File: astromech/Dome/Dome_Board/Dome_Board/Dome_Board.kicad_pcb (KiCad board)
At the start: 2 copper layers, 177.8 x 111.8 mm, 12 parts, among them J1 Conn_01x02_Socket, J10 Conn_01x02_Socket, J2 Conn_01x02_Socket, J3 Conn_01x02_Socket, J4 Conn_01x03_Pin, J5 Conn_01x03_Pin, J6 Conn_01x03_Pin, J7 Conn_01x03_Pin, J8 Conn_01x03_Pin, J9 Conn_01x03_Pin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

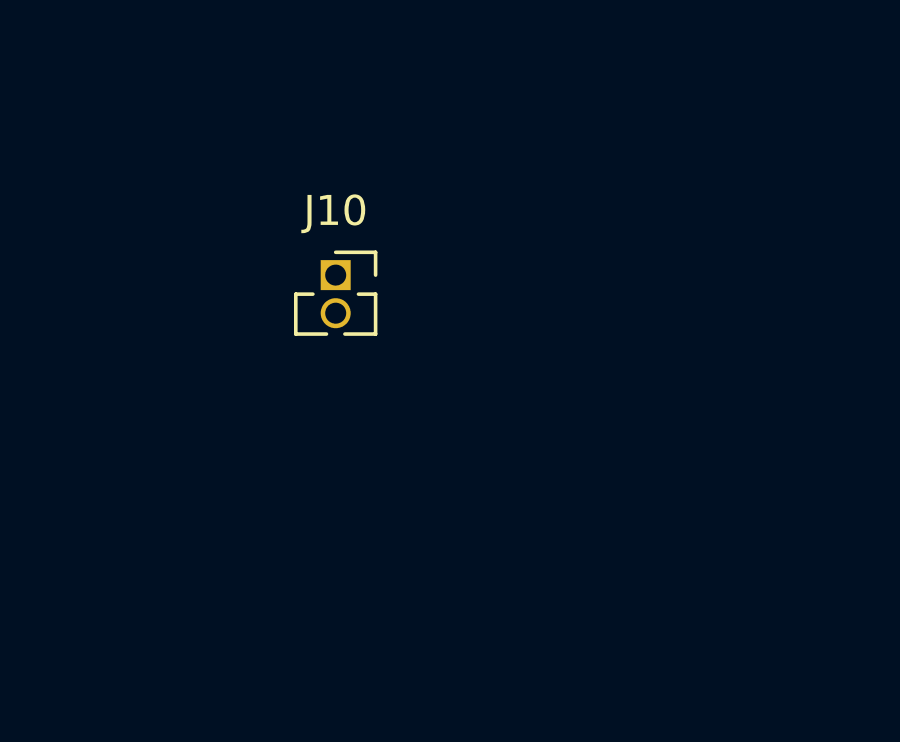
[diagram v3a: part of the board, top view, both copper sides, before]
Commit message: added low power txd, low power rxd, PWM connectors
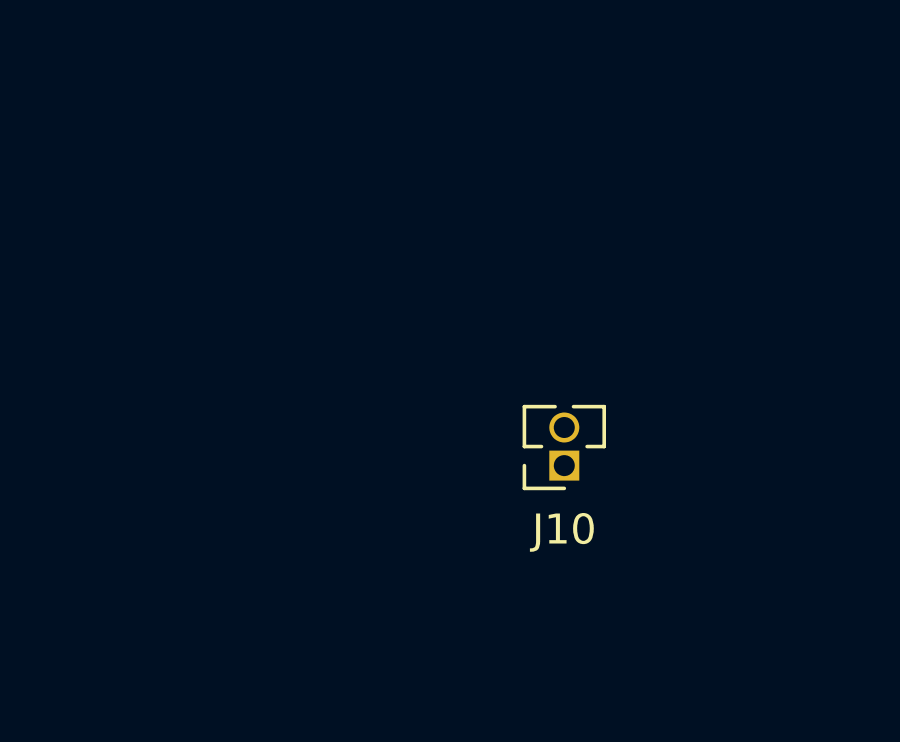
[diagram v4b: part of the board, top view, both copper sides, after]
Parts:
- moved J10 9.92 mm to (147.3, 73.7), turned to 180 degrees
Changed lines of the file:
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@@
 	(footprint "Connector_PinSocket_1.27mm:PinSocket_1x02_P1.27mm_Vertical"
 		(layer "F.Cu")
-		(at 139.7 67.31)
+		(at 147.32 73.66 180)
 		(descr "Through hole straight socket strip, 1x02, 1.27mm pitch, single row (from Kicad 4.0.7), script generated")
 		(tags "Through hole socket strip THT 1x02 1.27mm single row")
 		(property "Reference" "J10"
-			(at 0 -2.135 0)
+			(at 0 -2.135 360)
 			(layer "F.SilkS")
 			(effects
@@
 		)
 		(property "Value" "Conn_01x02_Socket"
-			(at 0 3.405 0)
+			(at 0 3.405 360)
 			(layer "F.Fab")
 			(effects
@@
 		)
 		(property "Footprint" "Connector_PinSocket_1.27mm:PinSocket_1x02_P1.27mm_Vertical"
-			(at 0 0 0)
+			(at 0 0 180)
 			(unlocked yes)
 			(layer "F.Fab")
@@
 		)
 		(property "Datasheet" ""
-			(at 0 0 0)
+			(at 0 0 180)
 			(unlocked yes)
 			(layer "F.Fab")
@@
 		)
 		(property "Description" ""
-			(at 0 0 0)
+			(at 0 0 180)
 			(unlocked yes)
 			(layer "F.Fab")
@@
 		(attr through_hole)
 		(fp_line
+			(start 1.33 0.635)
+			(end 1.33 1.965)
+			(stroke
+				(width 0.12)
+				(type solid)
+			)
+			(layer "F.SilkS")
+		)
+		(fp_line
+			(start 1.33 -0.76)
+			(end 1.33 0)
+			(stroke
+				(width 0.12)
+				(type solid)
+			)
+			(layer "F.SilkS")
+		)
+		(fp_line
+			(start 0.76 0.635)
+			(end 1.33 0.635)
+			(stroke
+				(width 0.12)
+				(type solid)
+			)
+			(layer "F.SilkS")
+		)
+		(fp_line
+			(start 0.30753 1.965)
+			(end 1.33 1.965)
+			(stroke
+				(width 0.12)
+				(type solid)
+			)
+			(layer "F.SilkS")
+		)
+		(fp_line
+			(start 0 -0.76)
+			(end 1.33 -0.76)
+			(stroke
+				(width 0.12)
+				(type solid)
+			)
+			(layer "F.SilkS")
+		)
+		(fp_line
+			(start -1.33 1.965)
+			(end -0.30753 1.965)
+			(stroke
+				(width 0.12)
+				(type solid)
+			)
+			(layer "F.SilkS")
+		)
+		(fp_line
+			(start -1.33 0.635)
+			(end -0.76 0.635)
+			(stroke
+				(width 0.12)
+				(type solid)
+			)
+			(layer "F.SilkS")
+		)
+		(fp_line
 			(start -1.33 0.635)
 			(end -1.33 1.965)
@@
 		)
 		(fp_line
-			(start -1.33 0.635)
-			(end -0.76 0.635)
-			(stroke
-				(width 0.12)
-				(type solid)
-			)
-			(layer "F.SilkS")
-		)
-		(fp_line
-			(start -1.33 1.965)
-			(end -0.30753 1.965)
-			(stroke
-				(width 0.12)
-				(type solid)
-			)
-			(layer "F.SilkS")
-		)
-		(fp_line
-			(start 0 -0.76)
-			(end 1.33 -0.76)
-			(stroke
-				(width 0.12)
-				(type solid)
-			)
-			(layer "F.SilkS")
-		)
-		(fp_line
-			(start 0.30753 1.965)
-			(end 1.33 1.965)
-			(stroke
-				(width 0.12)
-				(type solid)
-			)
-			(layer "F.SilkS")
-		)
-		(fp_line
-			(start 0.76 0.635)
-			(end 1.33 0.635)
-			(stroke
-				(width 0.12)
-				(type solid)
-			)
-			(layer "F.SilkS")
-		)
-		(fp_line
-			(start 1.33 -0.76)
-			(end 1.33 0)
-			(stroke
-				(width 0.12)
-				(type solid)
-			)
-			(layer "F.SilkS")
-		)
-		(fp_line
-			(start 1.33 0.635)
-			(end 1.33 1.965)
-			(stroke
-				(width 0.12)
-				(type solid)
-			)
-			(layer "F.SilkS")
+			(start 1.75 2.4)
+			(end -1.8 2.4)
+			(stroke
+				(width 0.05)
+				(type solid)
+			)
+			(layer "F.CrtYd")
+		)
+		(fp_line
+			(start 1.75 -1.15)
+			(end 1.75 2.4)
+			(stroke
+				(width 0.05)
+				(type solid)
+			)
+			(layer "F.CrtYd")
+		)
+		(fp_line
+			(start -1.8 2.4)
+			(end -1.8 -1.15)
+			(stroke
+				(width 0.05)
+				(type solid)
+			)
+			(layer "F.CrtYd")
 		)
 		(fp_line
@@
 		)
 		(fp_line
-			(start -1.8 2.4)
-			(end -1.8 -1.15)
-			(stroke
-				(width 0.05)
-				(type solid)
-			)
-			(layer "F.CrtYd")
-		)
-		(fp_line
-			(start 1.75 -1.15)
-			(end 1.75 2.4)
-			(stroke
-				(width 0.05)
-				(type solid)
-			)
-			(layer "F.CrtYd")
-		)
-		(fp_line
-			(start 1.75 2.4)
-			(end -1.8 2.4)
-			(stroke
-				(width 0.05)
-				(type solid)
-			)
-			(layer "F.CrtYd")
+			(start 1.27 1.905)
+			(end -1.27 1.905)
+			(stroke
+				(width 0.1)
+				(type solid)
+			)
+			(layer "F.Fab")
+		)
+		(fp_line
+			(start 1.27 0)
+			(end 1.27 1.905)
+			(stroke
+				(width 0.1)
+				(type solid)
+			)
+			(layer "F.Fab")
+		)
+		(fp_line
+			(start 0.635 -0.635)
+			(end 1.27 0)
+			(stroke
+				(width 0.1)
+				(type solid)
+			)
+			(layer "F.Fab")
+		)
+		(fp_line
+			(start -1.27 1.905)
+			(end -1.27 -0.635)
+			(stroke
+				(width 0.1)
+				(type solid)
+			)
+			(layer "F.Fab")
 		)
 		(fp_line
@@
 			(layer "F.Fab")
 		)
-		(fp_line
-			(start -1.27 1.905)
-			(end -1.27 -0.635)
-			(stroke
-				(width 0.1)
-				(type solid)
-			)
-			(layer "F.Fab")
-		)
-		(fp_line
-			(start 0.635 -0.635)
-			(end 1.27 0)
-			(stroke
-				(width 0.1)
-				(type solid)
-			)
-			(layer "F.Fab")
-		)
-		(fp_line
-			(start 1.27 0)
-			(end 1.27 1.905)
-			(stroke
-				(width 0.1)
-				(type solid)
-			)
-			(layer "F.Fab")
-		)
-		(fp_line
-			(start 1.27 1.905)
-			(end -1.27 1.905)
-			(stroke
-				(width 0.1)
-				(type solid)
-			)
-			(layer "F.Fab")
-		)
 		(fp_text user "${REFERENCE}"
 			(at 0 0.635 90)
@@
 		)
 		(pad "1" thru_hole rect
-			(at 0 0)
+			(at 0 0 180)
 			(size 1 1)
 			(drill 0.7)
@@
 		)
 		(pad "2" thru_hole oval
-			(at 0 1.27)
+			(at 0 1.27 180)
 			(size 1 1)
 			(drill 0.7)

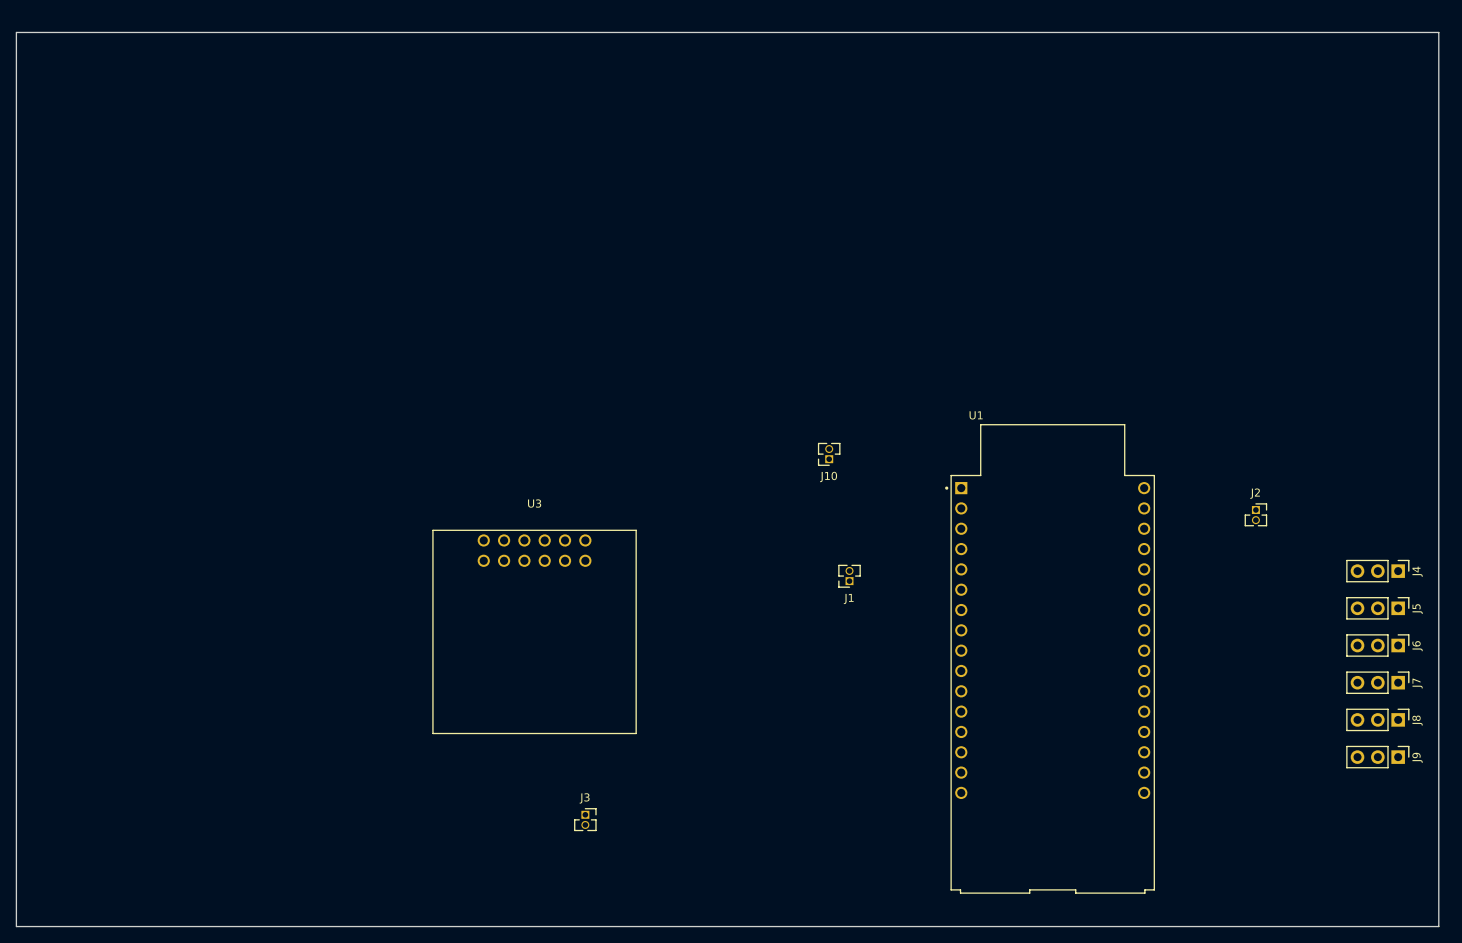
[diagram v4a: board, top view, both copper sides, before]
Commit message: added more PWM and Servo driver
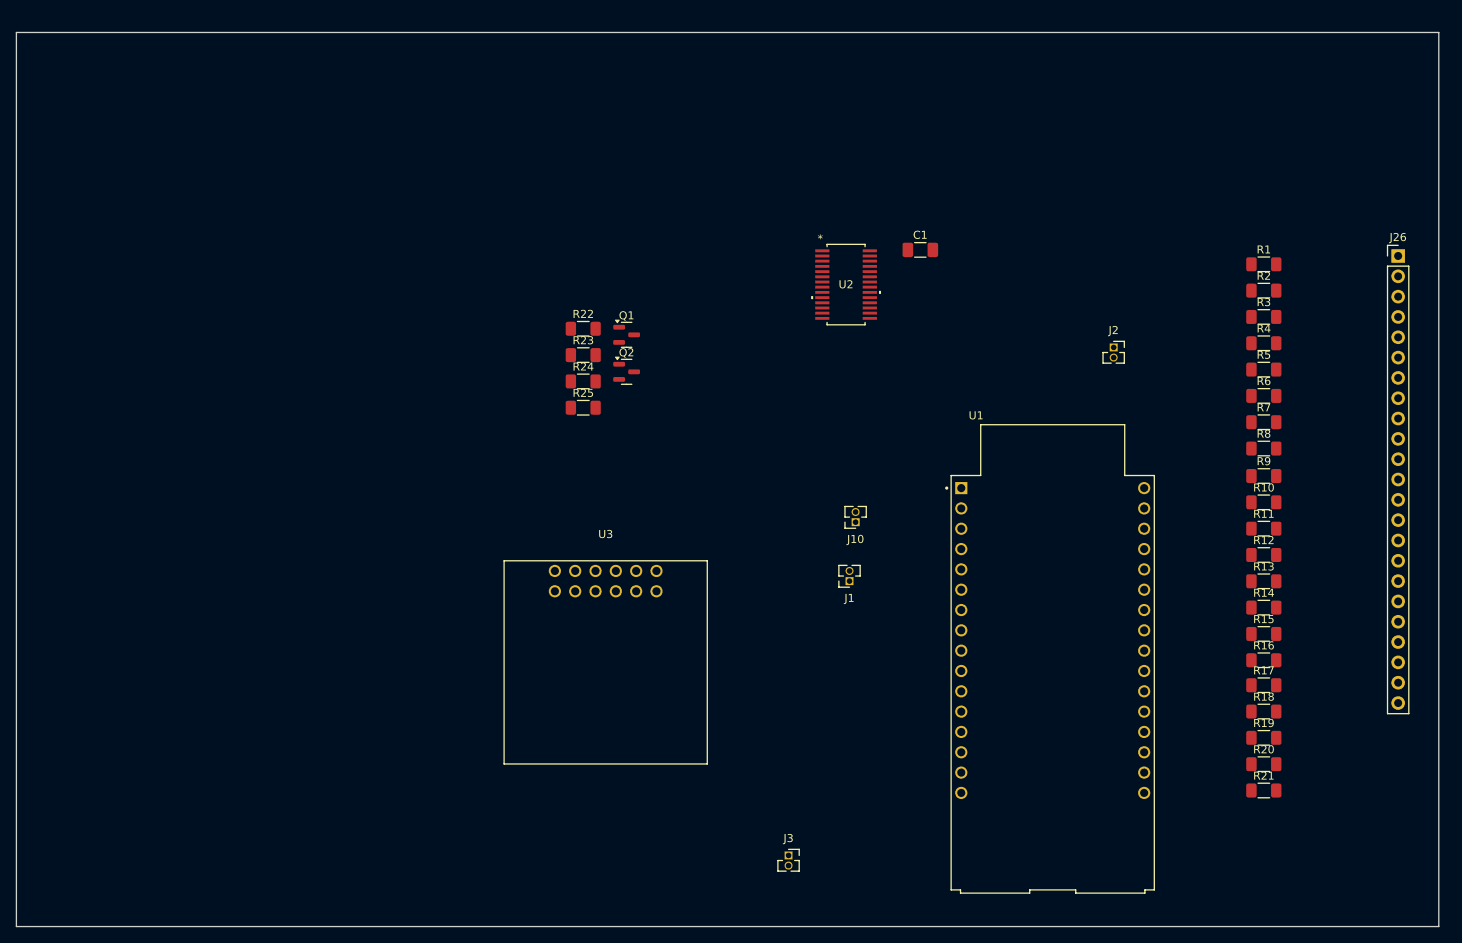
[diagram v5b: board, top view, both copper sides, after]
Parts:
- removed J4, J5, J6, J7, J8, J9: Conn_01x03_Pin, Connector_PinHeader_2.54mm:PinHeader_1x03_P2.54mm_Vertical
- added C1: C, Capacitor_SMD:C_1206_3216Metric_Pad1.33x1.80mm_HandSolder, F.Cu at (158.7, 47.5)
- added J26: Conn_01x23_Pin, Connector_PinHeader_2.54mm:PinHeader_1x23_P2.54mm_Vertical, F.Cu at (218.4, 48.3)
- added Q1: BSS138, Package_TO_SOT_SMD:SOT-23, F.Cu at (122.0, 58.1)
- added Q2: BSS138, Package_TO_SOT_SMD:SOT-23, F.Cu at (122.0, 62.7)
- added R1: R, Resistor_SMD:R_1206_3216Metric_Pad1.30x1.75mm_HandSolder, F.Cu at (201.7, 49.3)
- added R10: R, Resistor_SMD:R_1206_3216Metric_Pad1.30x1.75mm_HandSolder, F.Cu at (201.7, 79.1)
- added R11: R, Resistor_SMD:R_1206_3216Metric_Pad1.30x1.75mm_HandSolder, F.Cu at (201.7, 82.3)
- added R12: R, Resistor_SMD:R_1206_3216Metric_Pad1.30x1.75mm_HandSolder, F.Cu at (201.7, 85.6)
- added R13: R, Resistor_SMD:R_1206_3216Metric_Pad1.30x1.75mm_HandSolder, F.Cu at (201.7, 88.9)
- added R14: R, Resistor_SMD:R_1206_3216Metric_Pad1.30x1.75mm_HandSolder, F.Cu at (201.7, 92.2)
- added R15: R, Resistor_SMD:R_1206_3216Metric_Pad1.30x1.75mm_HandSolder, F.Cu at (201.7, 95.5)
- added R16: R, Resistor_SMD:R_1206_3216Metric_Pad1.30x1.75mm_HandSolder, F.Cu at (201.7, 98.8)
- added R17: R, Resistor_SMD:R_1206_3216Metric_Pad1.30x1.75mm_HandSolder, F.Cu at (201.7, 101.9)
- added R18: R, Resistor_SMD:R_1206_3216Metric_Pad1.30x1.75mm_HandSolder, F.Cu at (201.7, 105.2)
- added R19: R, Resistor_SMD:R_1206_3216Metric_Pad1.30x1.75mm_HandSolder, F.Cu at (201.7, 108.5)
- added R2: R, Resistor_SMD:R_1206_3216Metric_Pad1.30x1.75mm_HandSolder, F.Cu at (201.7, 52.6)
- added R20: R, Resistor_SMD:R_1206_3216Metric_Pad1.30x1.75mm_HandSolder, F.Cu at (201.7, 111.8)
- added R21: R, Resistor_SMD:R_1206_3216Metric_Pad1.30x1.75mm_HandSolder, F.Cu at (201.7, 115.1)
- added R22: R, Resistor_SMD:R_1206_3216Metric_Pad1.30x1.75mm_HandSolder, F.Cu at (116.6, 57.4)
- added R23: R, Resistor_SMD:R_1206_3216Metric_Pad1.30x1.75mm_HandSolder, F.Cu at (116.6, 60.6)
- added R24: R, Resistor_SMD:R_1206_3216Metric_Pad1.30x1.75mm_HandSolder, F.Cu at (116.6, 63.9)
- added R25: R, Resistor_SMD:R_1206_3216Metric_Pad1.30x1.75mm_HandSolder, F.Cu at (116.6, 67.2)
- added R3: R, Resistor_SMD:R_1206_3216Metric_Pad1.30x1.75mm_HandSolder, F.Cu at (201.7, 55.9)
- added R4: R, Resistor_SMD:R_1206_3216Metric_Pad1.30x1.75mm_HandSolder, F.Cu at (201.7, 59.2)
- added R5: R, Resistor_SMD:R_1206_3216Metric_Pad1.30x1.75mm_HandSolder, F.Cu at (201.7, 62.5)
- added R6: R, Resistor_SMD:R_1206_3216Metric_Pad1.30x1.75mm_HandSolder, F.Cu at (201.7, 65.8)
- added R7: R, Resistor_SMD:R_1206_3216Metric_Pad1.30x1.75mm_HandSolder, F.Cu at (201.7, 69.0)
- added R8: R, Resistor_SMD:R_1206_3216Metric_Pad1.30x1.75mm_HandSolder, F.Cu at (201.7, 72.3)
- added R9: R, Resistor_SMD:R_1206_3216Metric_Pad1.30x1.75mm_HandSolder, F.Cu at (201.7, 75.8)
- added U2: PCA9685PW, custom_library:SOT361-1_NXP-M, F.Cu at (149.4, 51.8)
- moved J2 27.0 mm to (182.9, 59.7)
- moved J3 25.9 mm to (142.2, 123.2)
- moved U3 9.67 mm to (119.4, 99.1)
- moved J10 8.54 mm to (150.6, 81.5)
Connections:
- U1 pad J1_1: unconnected-(U1-ESP_3V3-PadJ1_1) -> 3V3
- U1 pad J3_10: PWM 6 -> unconnected-(U1-GPIO18-PadJ3_10)
- U1 pad J3_4: unconnected-(U1-GPIO15-PadJ3_4) -> PWM 1
- U1 pad J3_5: PWM 1 -> PWM 2
- U1 pad J3_6: PWM 2 -> PWM 3
- U1 pad J3_7: PWM 3 -> PWM 4
- U1 pad J3_8: PWM 4 -> PWM 5
- U1 pad J3_9: PWM 5 -> unconnected-(U1-GPIO19-PadJ3_9)

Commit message: added reset button
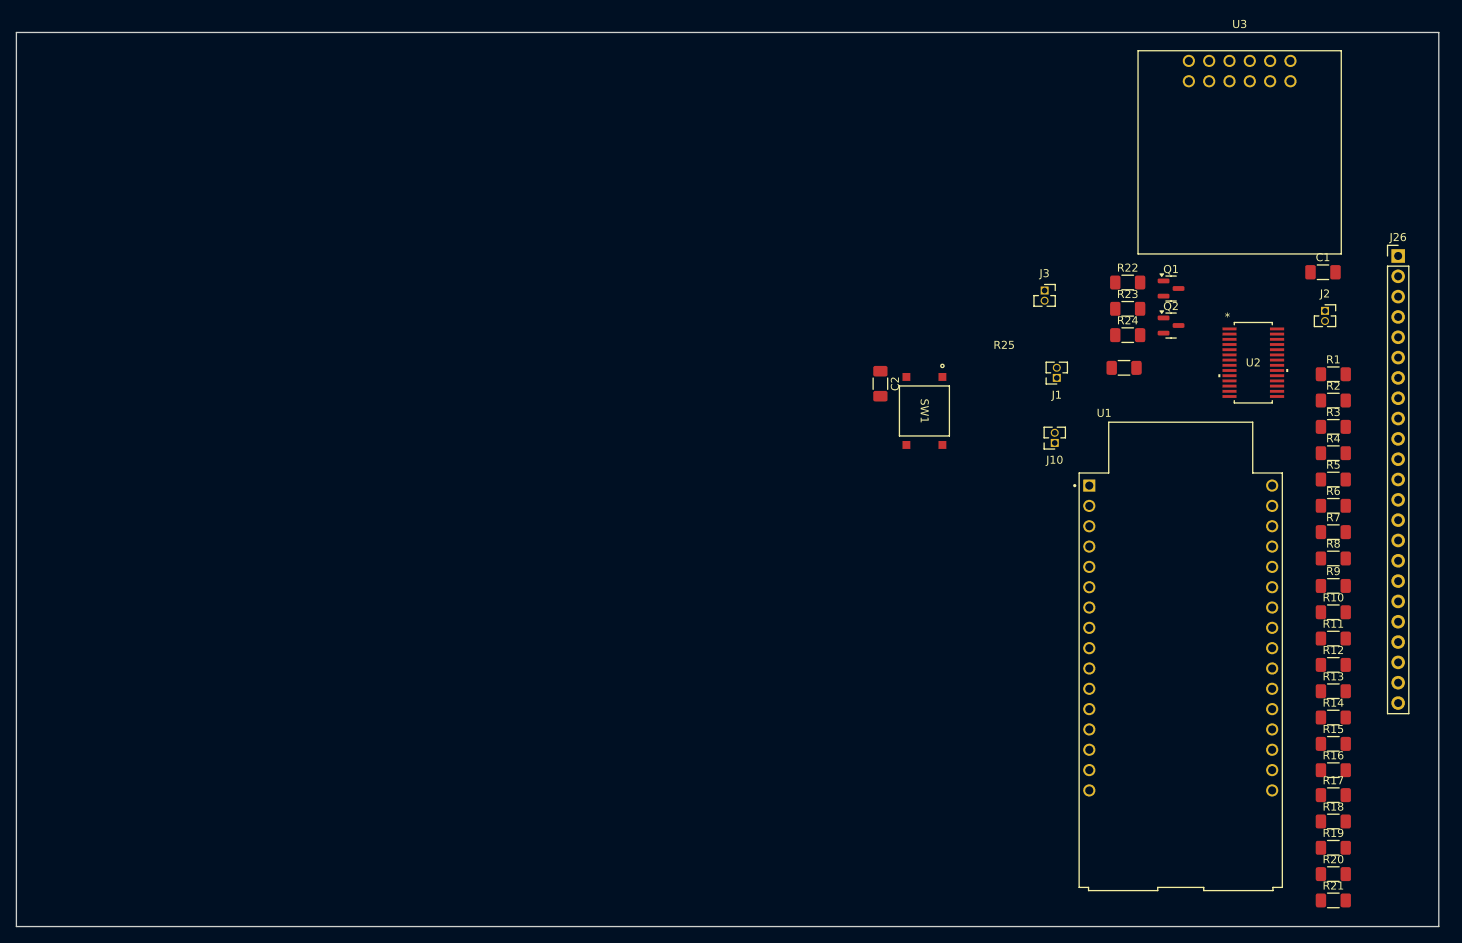
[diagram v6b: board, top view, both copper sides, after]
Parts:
- added C2: NC/100nF, Capacitor_SMD:C_1206_3216Metric_Pad1.33x1.80mm_HandSolder, F.Cu at (153.7, 64.2)
- added SW1: COM-12992, custom_library:COM-12992_SPK, F.Cu at (159.2, 67.6)
- moved U3 101.7 mm to (198.6, 35.3)
- moved J3 77.5 mm to (174.2, 52.6)
- moved R22 68.3 mm to (184.6, 51.6)
- moved R23 68.3 mm to (184.6, 54.9)
- moved R24 68.3 mm to (184.6, 58.2)
- moved Q1 68.3 mm to (190.1, 52.3)
- moved Q2 68.3 mm to (190.1, 57.0)
- moved R25 67.8 mm to (184.2, 62.2)
- moved U2 51.8 mm to (200.3, 61.6)
- moved C1 50.4 mm to (209.0, 50.3)
- moved J1 36.3 mm to (175.8, 63.5)
- moved J2 26.8 mm to (209.3, 55.1)
- moved J10 26.8 mm to (175.5, 71.6)
- moved R11 16.3 mm to (210.3, 96.1)
- moved R16 16.3 mm to (210.3, 112.5)
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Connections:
- net level converter magic renamed SDA +5V
- net more level converter magic renamed SCL +5V
- U1 pad J1_2: unconnected-(U1-CHIP_PU-PadJ1_2) -> rst_button
